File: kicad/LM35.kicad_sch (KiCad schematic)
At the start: 3 parts, among them J6 Microboard terminal

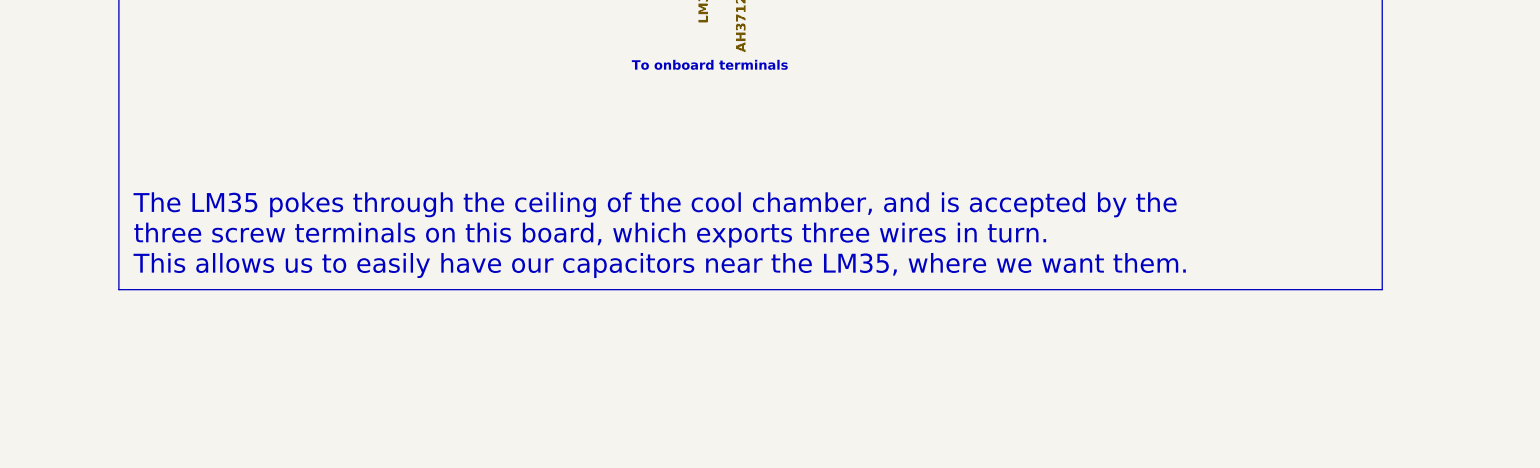
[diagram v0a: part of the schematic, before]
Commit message: kicad: use hand-solderable 0805s
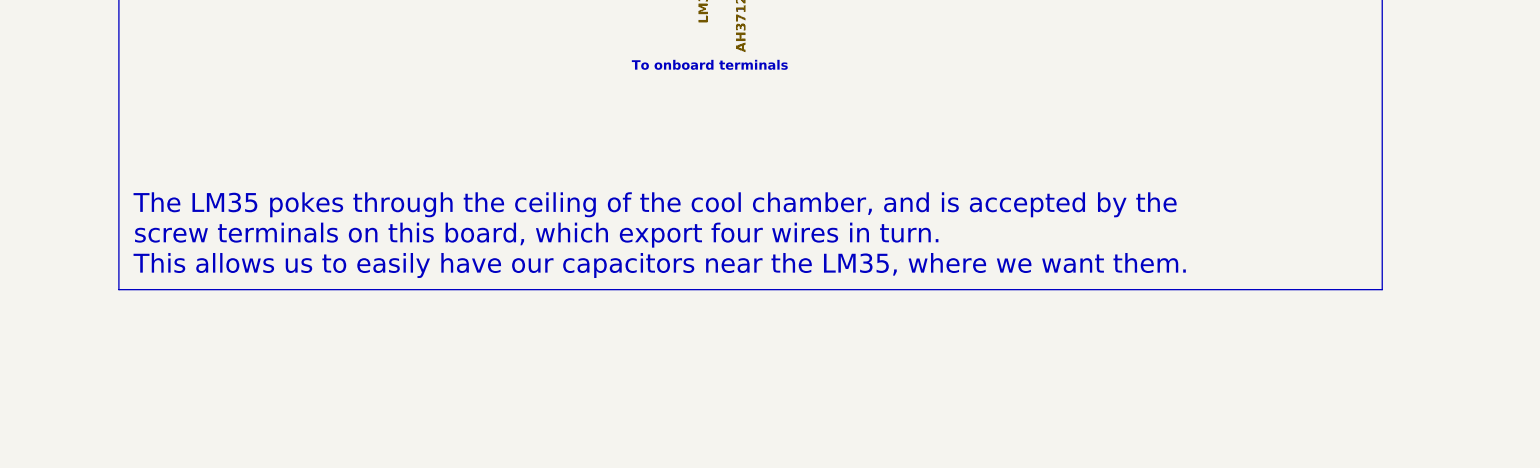
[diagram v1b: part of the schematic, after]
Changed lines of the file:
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@@
 		)
 	)
-	(text_box "The LM35 pokes through the ceiling of the cool chamber, and is accepted by the three screw terminals on this board, which exports three wires in turn.\nThis allows us to easily have our capacitors near the LM35, where we want them."
+	(text_box "The LM35 pokes through the ceiling of the cool chamber, and is accepted by the screw terminals on this board, which export four wires in turn.\nThis allows us to easily have our capacitors near the LM35, where we want them."
 		(exclude_from_sim no)
 		(at 45.72 38.1 0)

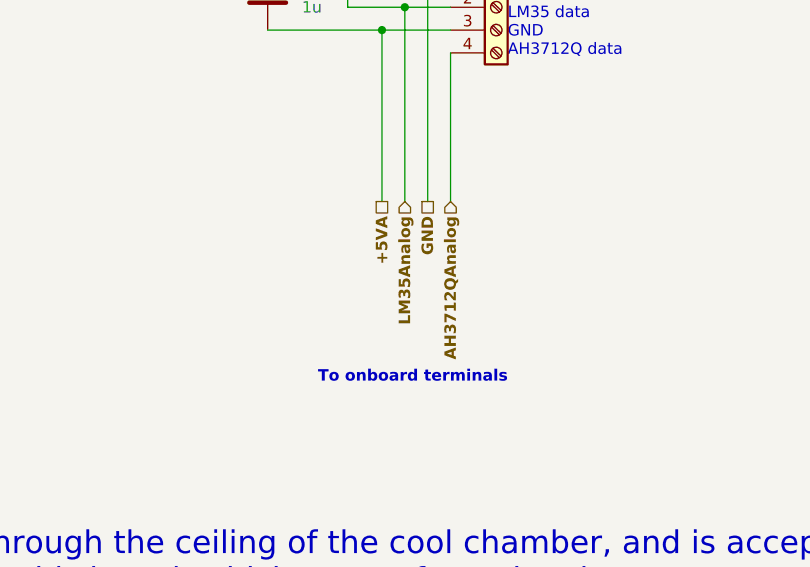
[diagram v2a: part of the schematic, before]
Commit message: kicad: need 412/680 voltage dividers on microboard data signals
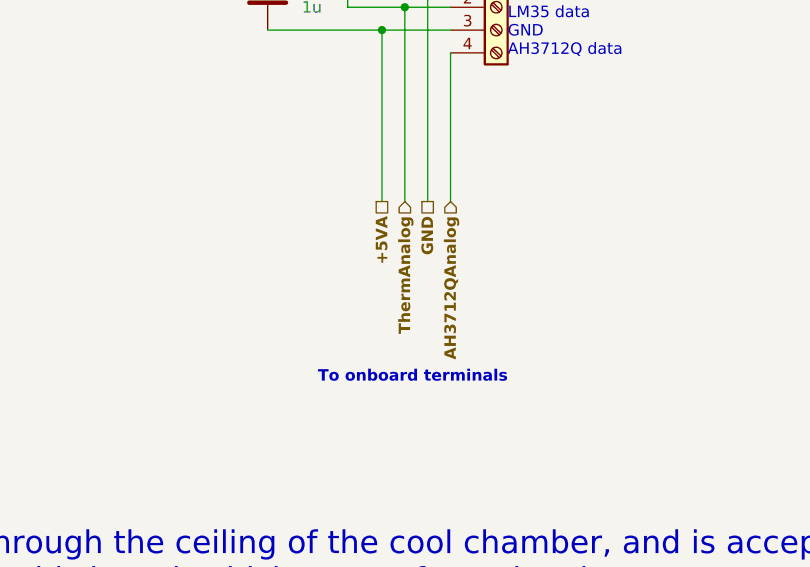
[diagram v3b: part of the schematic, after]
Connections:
- net LM35Analog renamed ThermAnalog
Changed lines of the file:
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@@
 		)
 	)
-	(hierarchical_label "LM35Analog"
+	(hierarchical_label "ThermAnalog"
 		(shape input)
 		(at 124.46 100.33 270)

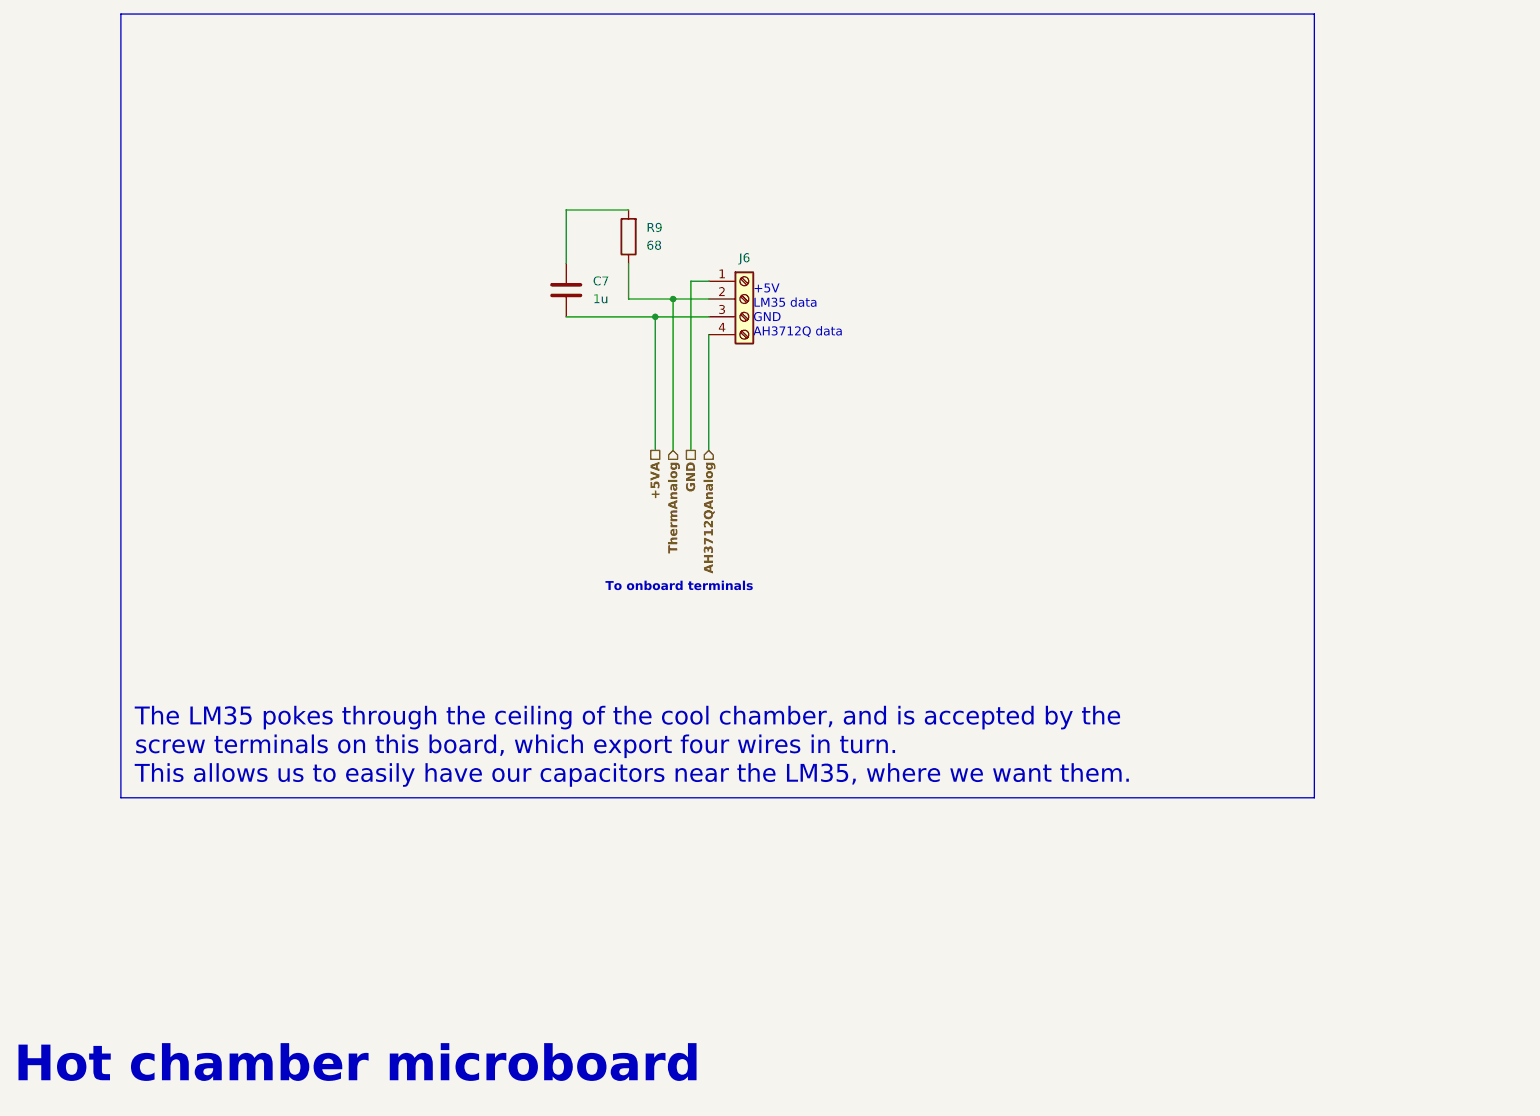
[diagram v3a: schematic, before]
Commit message: kicad: all throughhole in microboard
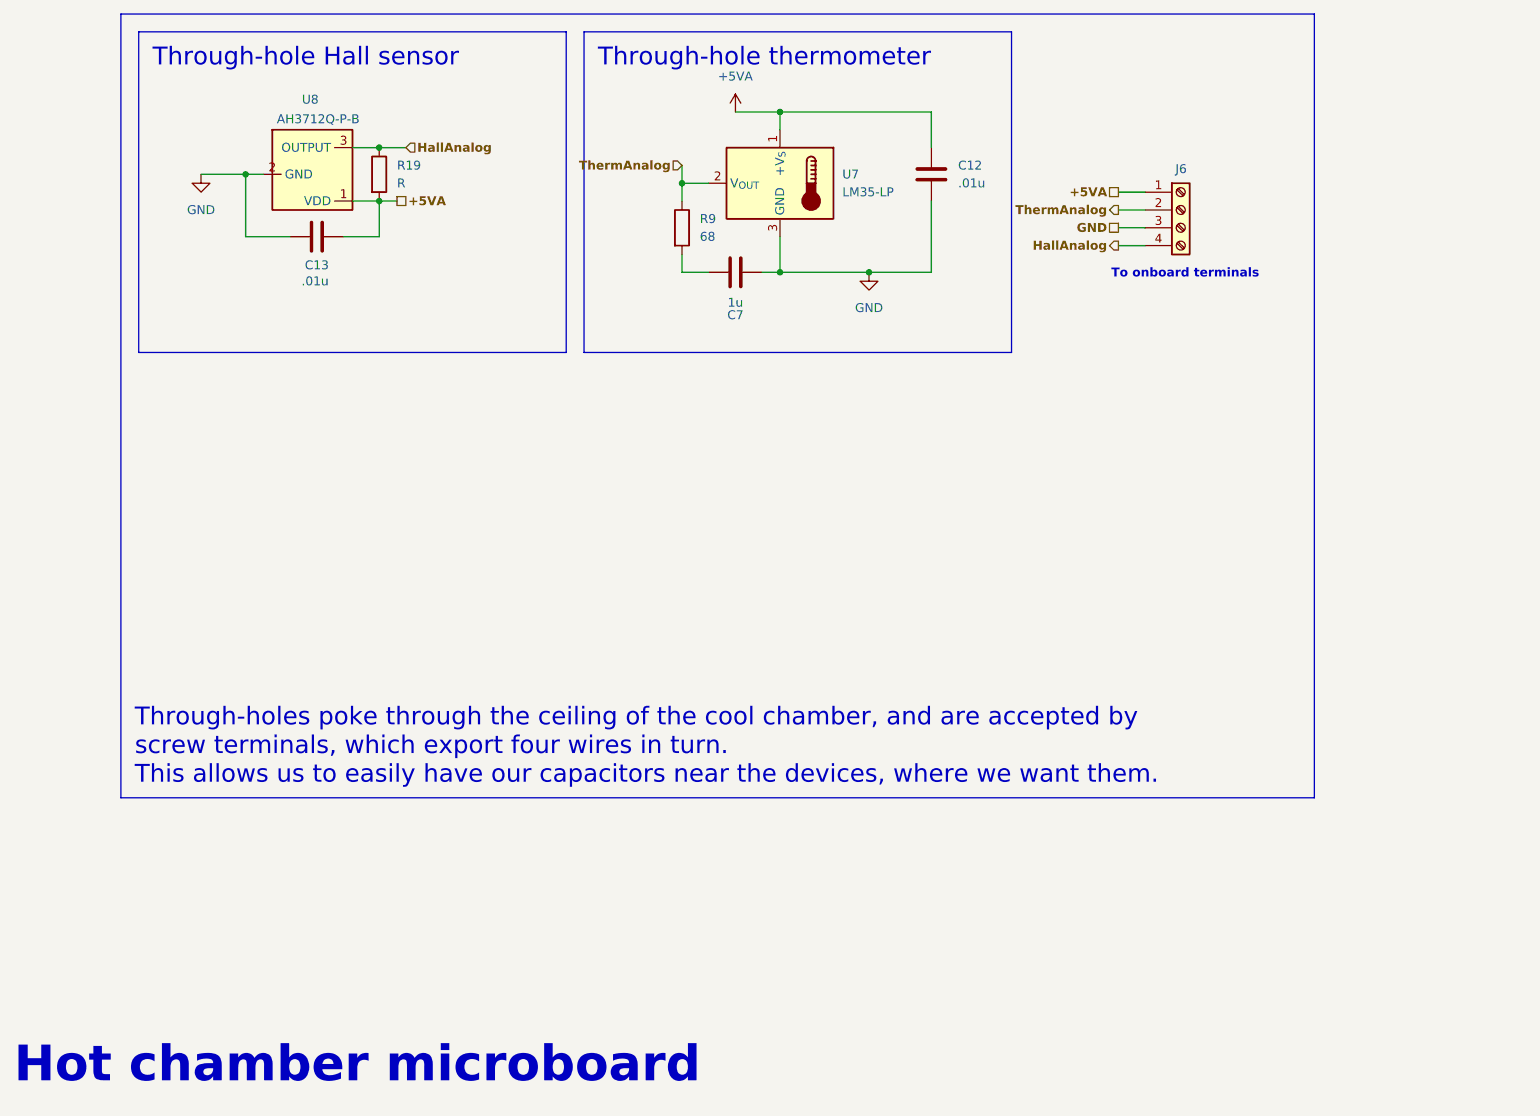
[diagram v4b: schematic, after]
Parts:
- added C12: .01u, Capacitor_SMD:C_0805_2012Metric_Pad1.18x1.45mm_HandSolder, symbol Device:C
- added C13: .01u, symbol Device:C
- added R19: R, symbol Device:R
- added U7: LM35-LP, Package_TO_SOT_THT:TO-92_Inline, symbol Sensor_Temperature:LM35-LP
- added U8: AH3712Q-P-B, Package_TO_SOT_SMD:SC-59, symbol dank:AH3712Q-P-B
- C7, R9: footprint (none) -> Capacitor_SMD:C_0805_2012Metric_Pad1.18x1.45mm_HandSolder
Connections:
- net +5VA: now also J6.1 (Pin_1), C12.1, C13.2, R19.2, U7.1 (+V_{S}), U8.1 (VDD); no longer C7.2, J6.3 (Pin_3)
- net GND: now also C7.1, J6.3 (Pin_3), C12.2, C13.1, U7.3 (GND), U8.2 (GND); no longer J6.1 (Pin_1)
- net ThermAnalog: now also U7.2 (V_{OUT})
- net at R9.2: now also C7.2; no longer C7.1
- net AH3712QAnalog renamed HallAnalog
- net HallAnalog: now also R19.1, U8.3 (OUTPUT)
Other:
- note removed: "+5V LM35 data GND AH3712Q data"
- moved on the sheet: J6

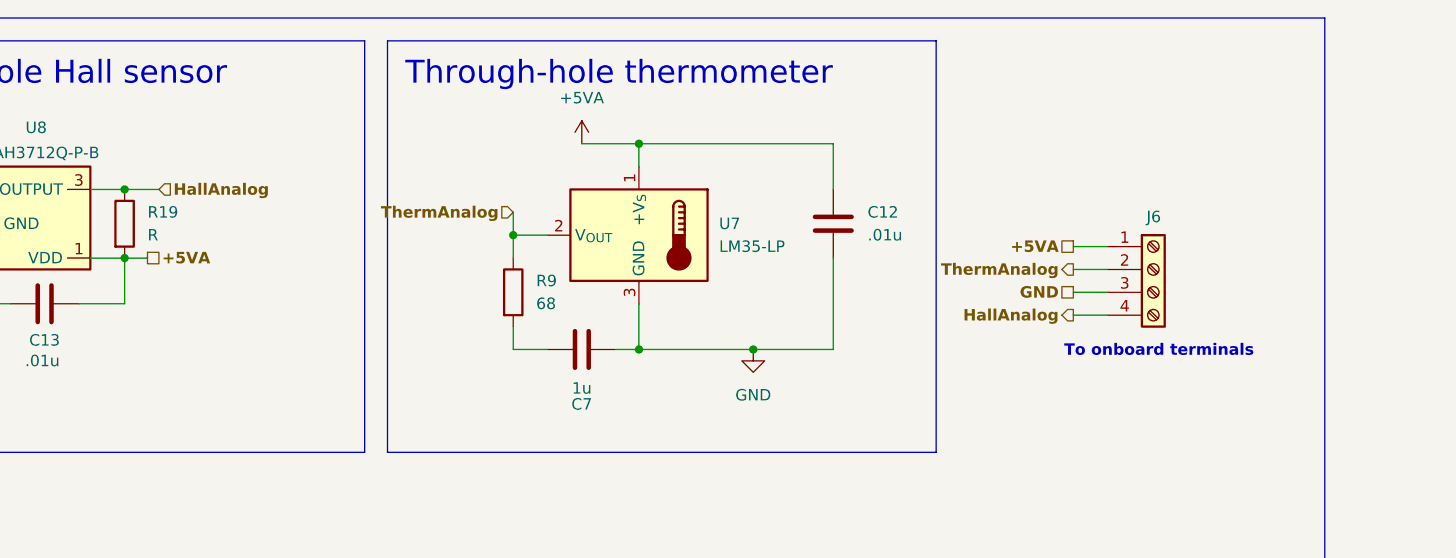
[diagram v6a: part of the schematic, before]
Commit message: take 3.3V to microboard rather than dividing 5V on return from hall sensor
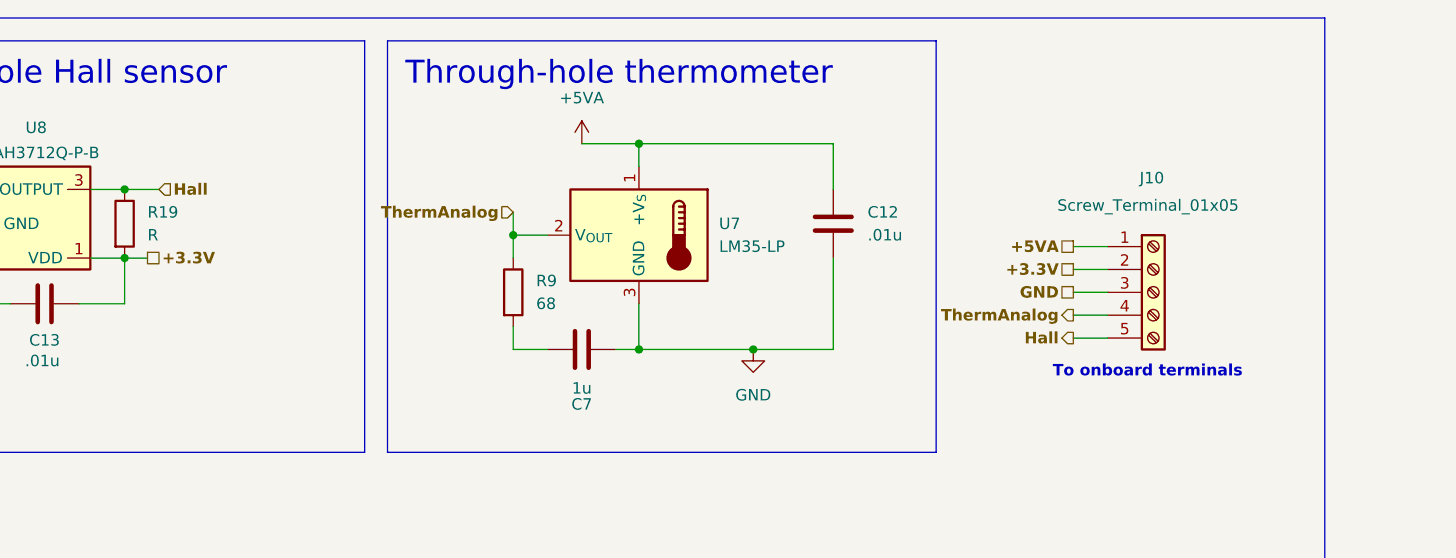
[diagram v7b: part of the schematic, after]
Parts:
- removed J6: Microboard terminal, symbol Connector:Screw_Terminal_01x04
- added J10: Screw_Terminal_01x05, dank:TerminalBlock_bornier-5_P5.08mm, symbol Connector:Screw_Terminal_01x05
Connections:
- net +5VA: now also J10.1 (Pin_1); no longer C13.2, R19.2, U8.1 (VDD)
- net GND: now also J10.3 (Pin_3)
- net ThermAnalog: now also J10.4 (Pin_4)
- net HallAnalog renamed Hall
- net Hall: now also J10.5 (Pin_5)
- new net +3.3V: C13.2, J10.2 (Pin_2), R19.2, U8.1 (VDD)
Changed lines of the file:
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@@
+	(wire
+		(pts
+			(xy 187.96 73.66) (xy 191.77 73.66)
+		)
+		(stroke
+			(width 0)
+			(type default)
+		)
+	)
 	(wire
 		(pts
@@
 	(text "To onboard terminals"
 		(exclude_from_sim no)
-		(at 186.944 75.184 0)
+		(at 185.674 77.47 0)
 		(effects
 			(font
@@
 		)
 	)
-	(hierarchical_label "HallAnalog"
-		(shape output)
-		(at 187.96 71.12 180)
+	(hierarchical_label "+3.3V"
+		(shape passive)
+		(at 187.96 66.04 180)
 		(fields_autoplaced yes)
 		(effects
@@
 		)
 	)
+	(hierarchical_label "Hall"
+		(shape output)
+		(at 187.96 73.66 180)
+		(fields_autoplaced yes)
+		(effects
+			(font
+				(size 1.27 1.27)
+				(thickness 0.254)
+				(bold yes)
+			)
+			(justify right)
+		)
+	)
 	(hierarchical_label "GND"
 		(shape passive)
@@
 		)
 	)
-	(hierarchical_label "HallAnalog"
+	(hierarchical_label "Hall"
 		(shape input)
 		(at 86.36 57.15 0)
@@
 		)
 	)
+	(hierarchical_label "+3.3V"
+		(shape passive)
+		(at 85.09 64.77 0)
+		(fields_autoplaced yes)
+		(effects
+			(font
+				(size 1.27 1.27)
+				(thickness 0.254)
+				(bold yes)
+			)
+			(justify left)
+		)
+	)
 	(hierarchical_label "ThermAnalog"
 		(shape output)
-		(at 187.96 66.04 180)
+		(at 187.96 71.12 180)
 		(fields_autoplaced yes)
 		(effects
@@
 			)
 			(justify right)
-		)
-	)
-	(hierarchical_label "+5VA"
-		(shape passive)
-		(at 85.09 64.77 0)
-		(fields_autoplaced yes)
-		(effects
-			(font
-				(size 1.27 1.27)
-				(thickness 0.254)
-				(bold yes)
-			)
-			(justify left)
 		)
 	)
@@
 	)
 	(symbol
-		(lib_id "Connector:Screw_Terminal_01x04")
-		(at 196.85 66.04 0)
-		(unit 1)
-		(exclude_from_sim no)
-		(in_bom yes)
-		(on_board no)
-		(dnp no)
-		(property "Reference" "J6"
-			(at 196.088 60.198 0)
-			(effects
-				(font
-					(size 1.27 1.27)
-				)
-				(justify left)
-			)
-		)
-		(property "Value" "Microboard terminal"
-			(at 201.422 75.946 0)
-			(effects
-				(font
-					(size 1.27 1.27)
-				)
-				(justify left)
-				(hide yes)
-			)
-		)
-		(property "Footprint" ""
-			(at 196.85 66.04 0)
-			(effects
-				(font
-					(size 1.27 1.27)
-				)
-				(hide yes)
-			)
-		)
-		(property "Datasheet" "~"
-			(at 196.85 66.04 0)
-			(effects
-				(font
-					(size 1.27 1.27)
-				)
-				(hide yes)
-			)
-		)
-		(property "Description" "Generic screw terminal, single row, 01x04, script generated (kicad-library-utils/schlib/autogen/connector/)"
-			(at 196.85 66.04 0)
-			(effects
-				(font
-					(size 1.27 1.27)
-				)
-				(hide yes)
-			)
-		)
-		(pin "2"
-		)
-		(pin "1"
-		)
-		(pin "4"
-		)
-		(pin "3"
-		)
-		(instances
-			(project "dankdryer"
-				(path "/0e28ce9c-097a-4614-9b8c-9333a7b96611/7565128f-4bdc-4cc8-b00b-bbda48a41b13"
-					(reference "J6")
-					(unit 1)
-				)
-			)
-		)
-	)
-	(symbol
 		(lib_id "dank:AH3712Q-P-B")
 		(at 73.66 62.23 0)
@@
 					(unit 1)
 				)
+			)
+		)
+	)
+	(symbol
+		(lib_id "Connector:Screw_Terminal_01x05")
+		(at 196.85 68.58 0)
+		(unit 1)
+		(exclude_from_sim no)
+		(in_bom yes)
+		(on_board no)
+		(dnp no)
+		(property "Reference" "J10"
+			(at 195.326 55.88 0)
+			(effects
+				(font
+					(size 1.27 1.27)
+				)
+				(justify left)
+			)
+		)
+		(property "Value" "Screw_Terminal_01x05"
+			(at 186.182 58.928 0)
+			(effects
+				(font
+					(size 1.27 1.27)
+				)
+				(justify left)
+			)
+		)
+		(property "Footprint" "dank:TerminalBlock_bornier-5_P5.08mm"
+			(at 196.85 68.58 0)
+			(effects
+				(font
+					(size 1.27 1.27)
+				)
+				(hide yes)
+			)
+		)
+		(property "Datasheet" "~"
+			(at 196.85 68.58 0)
+			(effects
+				(font
+					(size 1.27 1.27)
+				)
+				(hide yes)
+			)
+		)
+		(property "Description" "Generic screw terminal, single row, 01x05, script generated (kicad-library-utils/schlib/autogen/connector/)"
+			(at 196.85 68.58 0)
+			(effects
+				(font
+					(size 1.27 1.27)
+				)
+				(hide yes)
+			)
+		)
+		(pin "1"
+		)
+		(pin "2"
+		)
+		(pin "3"
+		)
+		(pin "5"
+		)
+		(pin "4"
+		)
+		(instances
+			(project ""
+				(path "/0e28ce9c-097a-4614-9b8c-9333a7b96611/7565128f-4bdc-4cc8-b00b-bbda48a41b13"
+					(reference "J10")
+					(unit 1)
+				)
